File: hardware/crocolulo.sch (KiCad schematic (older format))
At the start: 2 parts

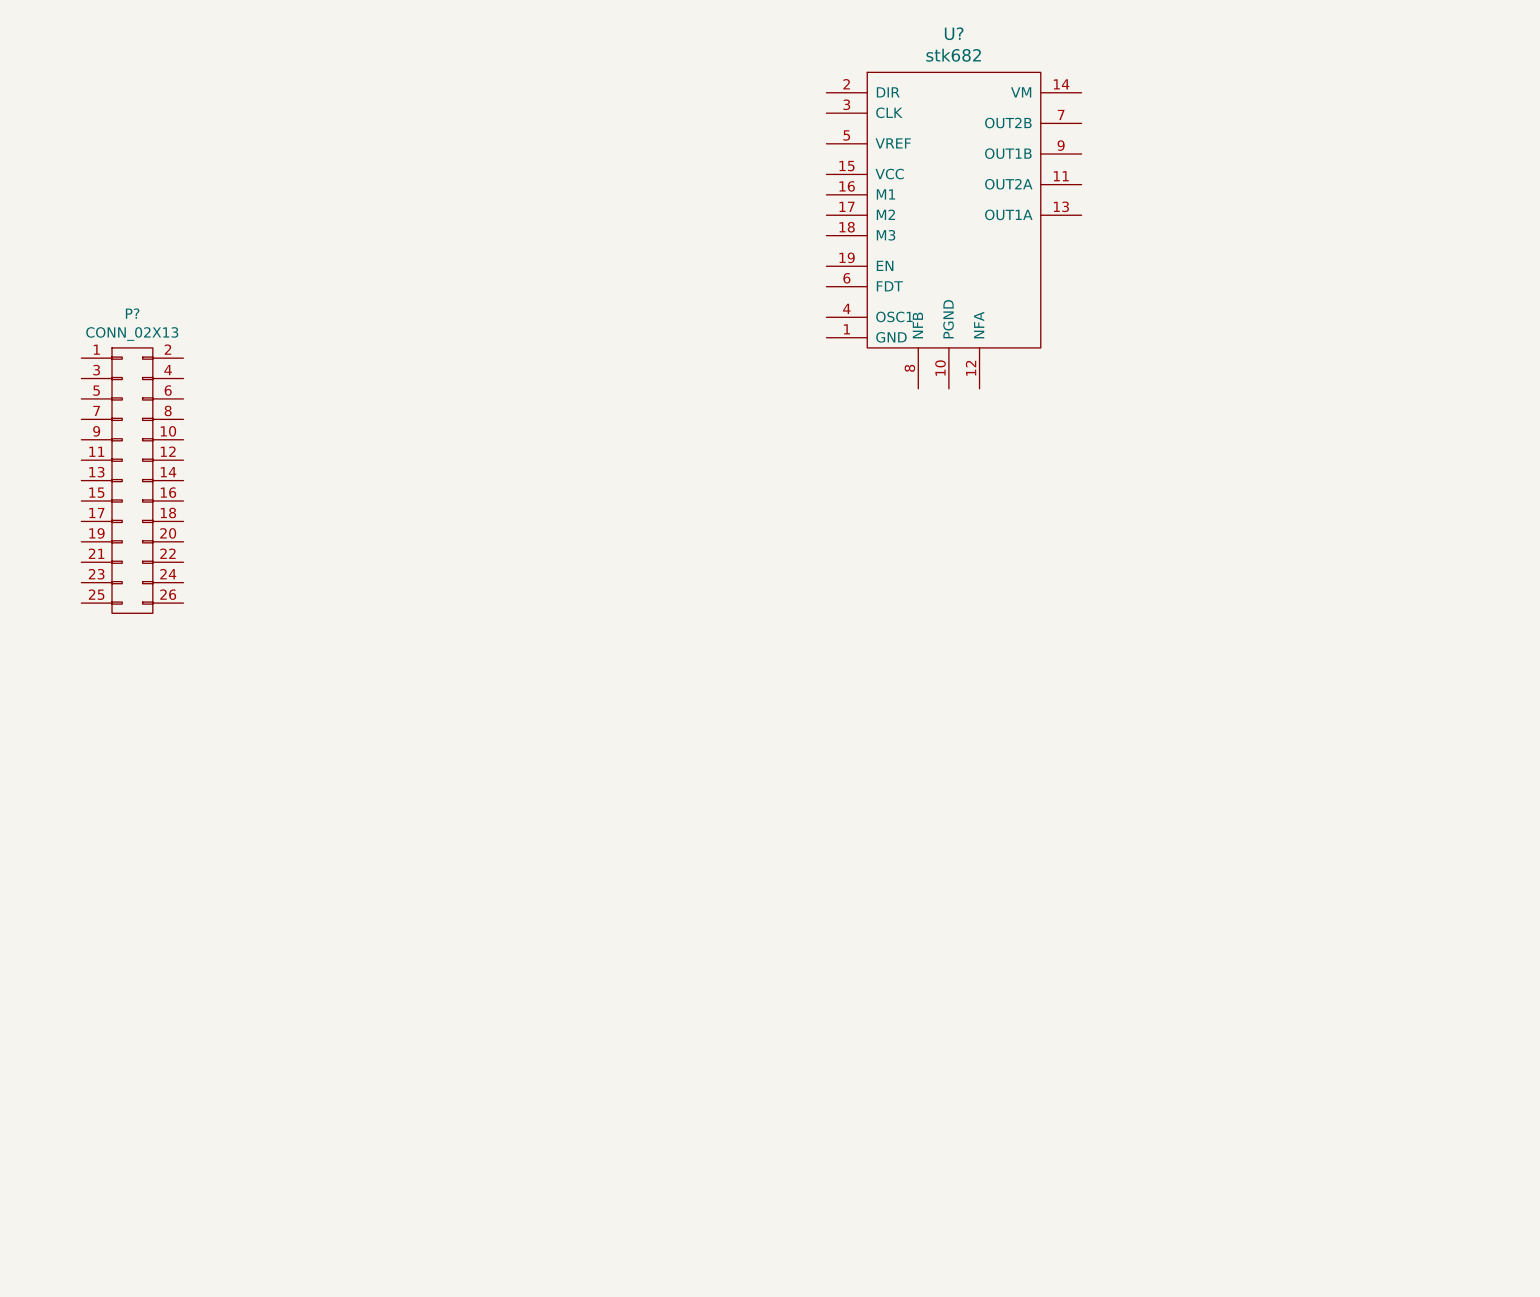
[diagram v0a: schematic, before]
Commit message: Add sub sheet to describe a single stepper driver module
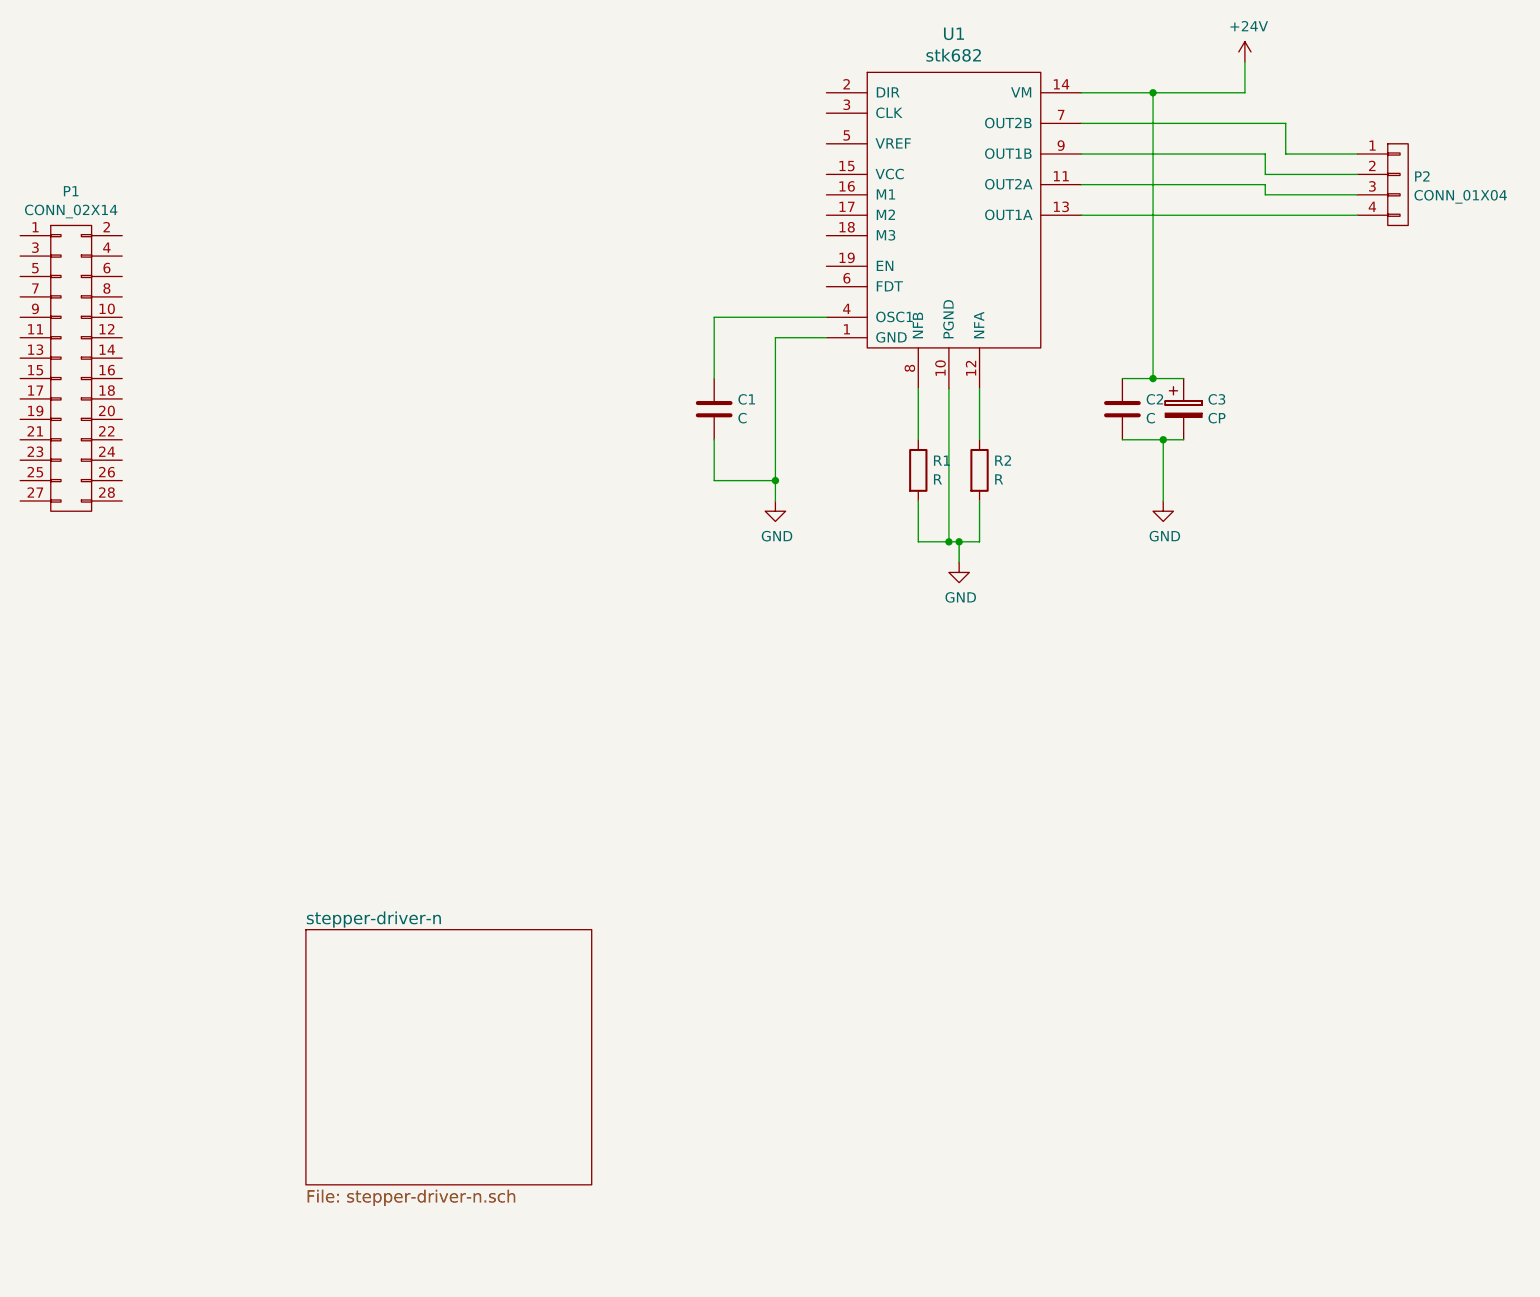
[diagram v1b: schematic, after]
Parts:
- removed P?: CONN_02X13, symbol CONN_02X13
- added C1, C2: C, symbol C
- added C3: CP, symbol CP
- added P1: CONN_02X14, symbol CONN_02X14
- added P2: CONN_01X04, symbol CONN_01X04
- added R1, R2: R, symbol R
- gave numbers to parts that had none: 1
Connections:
- net GND: now reaches U1.1 (GND)
- net GND: now also U1.10 (PGND), C1.2, C2.2, C3.2, R1.2, R2.2
- net at U1.11 (OUT2A): now also P2.3 (P3)
- net at U1.12 (NFA): now also R2.1
- net at U1.13 (OUT1A): now also P2.4 (P4)
- net +24V: now reaches U1.14 (VM)
- net +24V: now also C2.1, C3.1
- net at U1.4 (OSC1): now also C1.1
- net at U1.7 (OUT2B): now also P2.1 (P1)
- net at U1.8 (NFB): now also R1.1
- net at U1.9 (OUT1B): now also P2.2 (P2)
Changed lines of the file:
@@
 LIBS:valves
 LIBS:stk682
+LIBS:crocolulo-cache
 EELAYER 25 0
 EELAYER END
 $Descr A4 11693 8268
 encoding utf-8
-Sheet 1 1
+Sheet 1 2
 Title "Crocolulo Stepper Driver"
 Date ""
@@
 $EndDescr
 $Comp
-L stk682 U?
+L stk682 U1
 U 1 1 56C73EAB
 P 5850 1800
-F 0 "U?" H 5875 2587 60  0000 C CNN
+F 0 "U1" H 5875 2587 60  0000 C CNN
 F 1 "stk682" H 5875 2481 60  0000 C CNN
 F 2 "" H 5850 1800 60  0000 C CNN
@@
 $EndComp
 $Comp
-L CONN_02X13 P?
-U 1 1 56C741F5
-P 1850 3200
-F 0 "P?" H 1850 4016 50  0000 C CNN
-F 1 "CONN_02X13" H 1850 3924 50  0000 C CNN
-F 2 "" H 1850 2050 50  0000 C CNN
-F 3 "" H 1850 2050 50  0000 C CNN
-	1    1850 3200
-	1    0    0    -1
-$EndComp
+L C C1
+U 1 1 56C84AD0
+P 4700 2850
+F 0 "C1" H 4815 2896 50  0000 L CNN
+F 1 "C" H 4815 2804 50  0000 L CNN
+F 2 "" H 4738 2700 50  0000 C CNN
+F 3 "" H 4700 2850 50  0000 C CNN
+	1    4700 2850
+	1    0    0    -1
+$EndComp
+Wire Wire Line
+	4700 2700 4700 2400
+Wire Wire Line
+	4700 2400 5250 2400
+$Comp
+L GND #PWR1
+U 1 1 56C84B13
+P 5000 3300
+F 0 "#PWR1" H 5000 3050 50  0001 C CNN
+F 1 "GND" H 5008 3126 50  0000 C CNN
+F 2 "" H 5000 3300 50  0000 C CNN
+F 3 "" H 5000 3300 50  0000 C CNN
+	1    5000 3300
+	1    0    0    -1
+$EndComp
+Wire Wire Line
+	5000 3300 5000 2500
+Wire Wire Line
+	5000 2500 5250 2500
+Wire Wire Line
+	4700 3000 4700 3200
+Wire Wire Line
+	4700 3200 5000 3200
+Connection ~ 5000 3200
+$Comp
+L R R1
+U 1 1 56C84B3E
+P 5700 3150
+F 0 "R1" H 5770 3196 50  0000 L CNN
+F 1 "R" H 5770 3104 50  0000 L CNN
+F 2 "" V 5630 3150 50  0000 C CNN
+F 3 "" H 5700 3150 50  0000 C CNN
+	1    5700 3150
+	1    0    0    -1
+$EndComp
+$Comp
+L R R2
+U 1 1 56C84B76
+P 6000 3150
+F 0 "R2" H 6070 3196 50  0000 L CNN
+F 1 "R" H 6070 3104 50  0000 L CNN
+F 2 "" V 5930 3150 50  0000 C CNN
+F 3 "" H 6000 3150 50  0000 C CNN
+	1    6000 3150
+	1    0    0    -1
+$EndComp
+$Comp
+L GND #PWR2
+U 1 1 56C84B9A
+P 5900 3600
+F 0 "#PWR2" H 5900 3350 50  0001 C CNN
+F 1 "GND" H 5908 3426 50  0000 C CNN
+F 2 "" H 5900 3600 50  0000 C CNN
+F 3 "" H 5900 3600 50  0000 C CNN
+	1    5900 3600
+	1    0    0    -1
+$EndComp
+Wire Wire Line
+	6000 2750 6000 3000
+Wire Wire Line
+	5700 2750 5700 3000
+Wire Wire Line
+	5850 2750 5850 3500
+Wire Wire Line
+	5700 3500 6000 3500
+Wire Wire Line
+	5900 3500 5900 3600
+Wire Wire Line
+	5700 3300 5700 3500
+Connection ~ 5850 3500
+Wire Wire Line
+	6000 3500 6000 3300
+Connection ~ 5900 3500
+$Comp
+L CONN_01X04 P2
+U 1 1 56C84C17
+P 8050 1750
+F 0 "P2" H 8127 1788 50  0000 L CNN
+F 1 "CONN_01X04" H 8127 1696 50  0000 L CNN
+F 2 "" H 8050 1750 50  0000 C CNN
+F 3 "" H 8050 1750 50  0000 C CNN
+	1    8050 1750
+	1    0    0    -1
+$EndComp
+$Comp
+L +24V #PWR4
+U 1 1 56C84C67
+P 7300 1150
+F 0 "#PWR4" H 7300 1000 50  0001 C CNN
+F 1 "+24V" H 7318 1324 50  0000 C CNN
+F 2 "" H 7300 1150 50  0000 C CNN
+F 3 "" H 7300 1150 50  0000 C CNN
+	1    7300 1150
+	1    0    0    -1
+$EndComp
+Wire Wire Line
+	6500 1300 7300 1300
+Wire Wire Line
+	7300 1300 7300 1150
+Wire Wire Line
+	6500 1450 7500 1450
+Wire Wire Line
+	7500 1450 7500 1600
+Wire Wire Line
+	7500 1600 7850 1600
+Wire Wire Line
+	6500 1600 7400 1600
+Wire Wire Line
+	7400 1600 7400 1700
+Wire Wire Line
+	7400 1700 7850 1700
+Wire Wire Line
+	6500 1750 7400 1750
+Wire Wire Line
+	7400 1750 7400 1800
+Wire Wire Line
+	7400 1800 7850 1800
+Wire Wire Line
+	6500 1900 7850 1900
+$Comp
+L C C2
+U 1 1 56C84F28
+P 6700 2850
+F 0 "C2" H 6815 2896 50  0000 L CNN
+F 1 "C" H 6815 2804 50  0000 L CNN
+F 2 "" H 6738 2700 50  0000 C CNN
+F 3 "" H 6700 2850 50  0000 C CNN
+	1    6700 2850
+	1    0    0    -1
+$EndComp
+$Comp
+L CP C3
+U 1 1 56C84F62
+P 7000 2850
+F 0 "C3" H 7118 2896 50  0000 L CNN
+F 1 "CP" H 7118 2804 50  0000 L CNN
+F 2 "" H 7038 2700 50  0000 C CNN
+F 3 "" H 7000 2850 50  0000 C CNN
+	1    7000 2850
+	1    0    0    -1
+$EndComp
+Wire Wire Line
+	6700 2700 7000 2700
+Wire Wire Line
+	6850 2700 6850 1300
+Connection ~ 6850 1300
+Connection ~ 6850 2700
+Wire Wire Line
+	6700 3000 7000 3000
+$Comp
+L GND #PWR3
+U 1 1 56C85015
+P 6900 3300
+F 0 "#PWR3" H 6900 3050 50  0001 C CNN
+F 1 "GND" H 6908 3126 50  0000 C CNN
+F 2 "" H 6900 3300 50  0000 C CNN
+F 3 "" H 6900 3300 50  0000 C CNN
+	1    6900 3300
+	1    0    0    -1
+$EndComp
+Wire Wire Line
+	6900 3300 6900 3000
+Connection ~ 6900 3000
+$Comp
+L CONN_02X14 P1
+U 1 1 56C9E180
+P 1550 2650
+F 0 "P1" H 1550 3516 50  0000 C CNN
+F 1 "CONN_02X14" H 1550 3424 50  0000 C CNN
+F 2 "" H 1550 1500 50  0000 C CNN
+F 3 "" H 1550 1500 50  0000 C CNN
+	1    1550 2650
+	1    0    0    -1
+$EndComp
+$Sheet
+S 2700 5400 1400 1250
+U 56C9E55A
+F0 "stepper-driver-n" 60
+F1 "stepper-driver-n.sch" 60
+$EndSheet
 $EndSCHEMATC
